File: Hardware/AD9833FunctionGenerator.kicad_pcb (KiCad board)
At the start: 2 copper layers, 125.7 x 172.7 mm, 54 parts, among them U1 LM7805_TO220

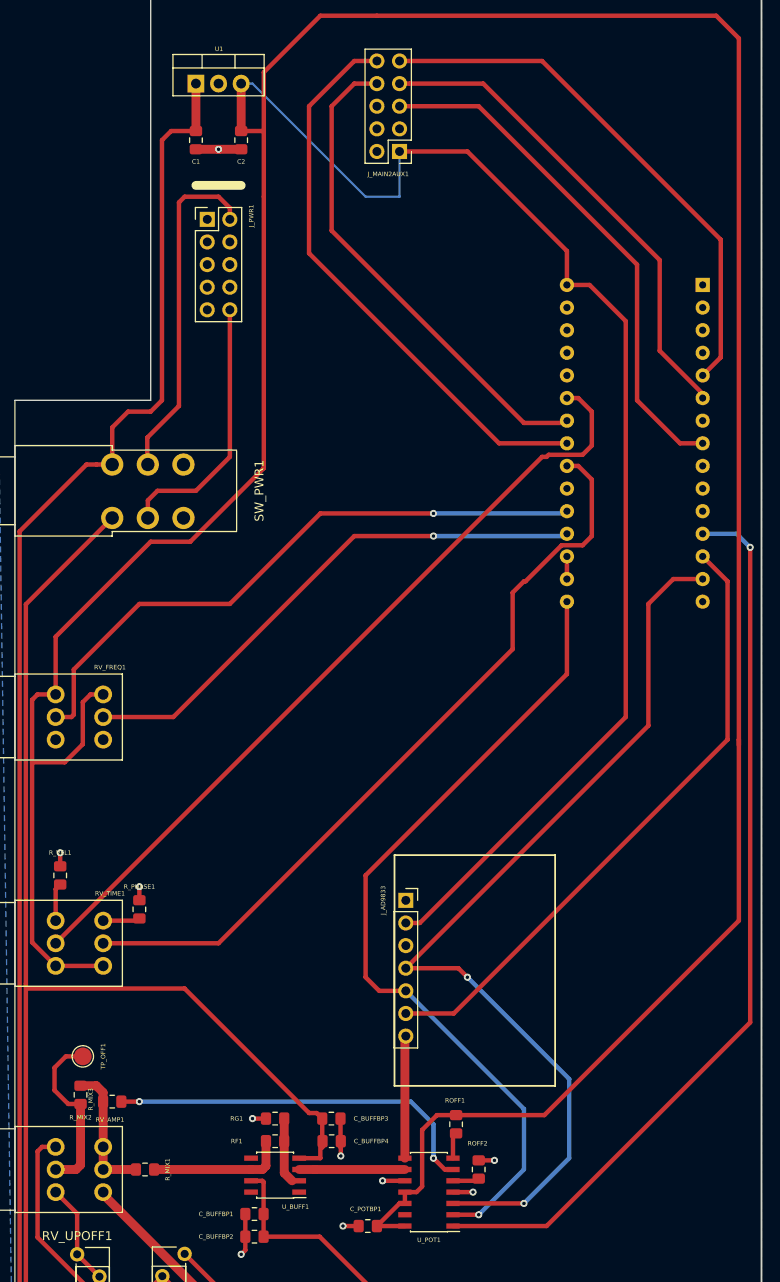
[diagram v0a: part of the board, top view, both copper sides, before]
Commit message: Repositioned Nano module so that USB socket faces upwards
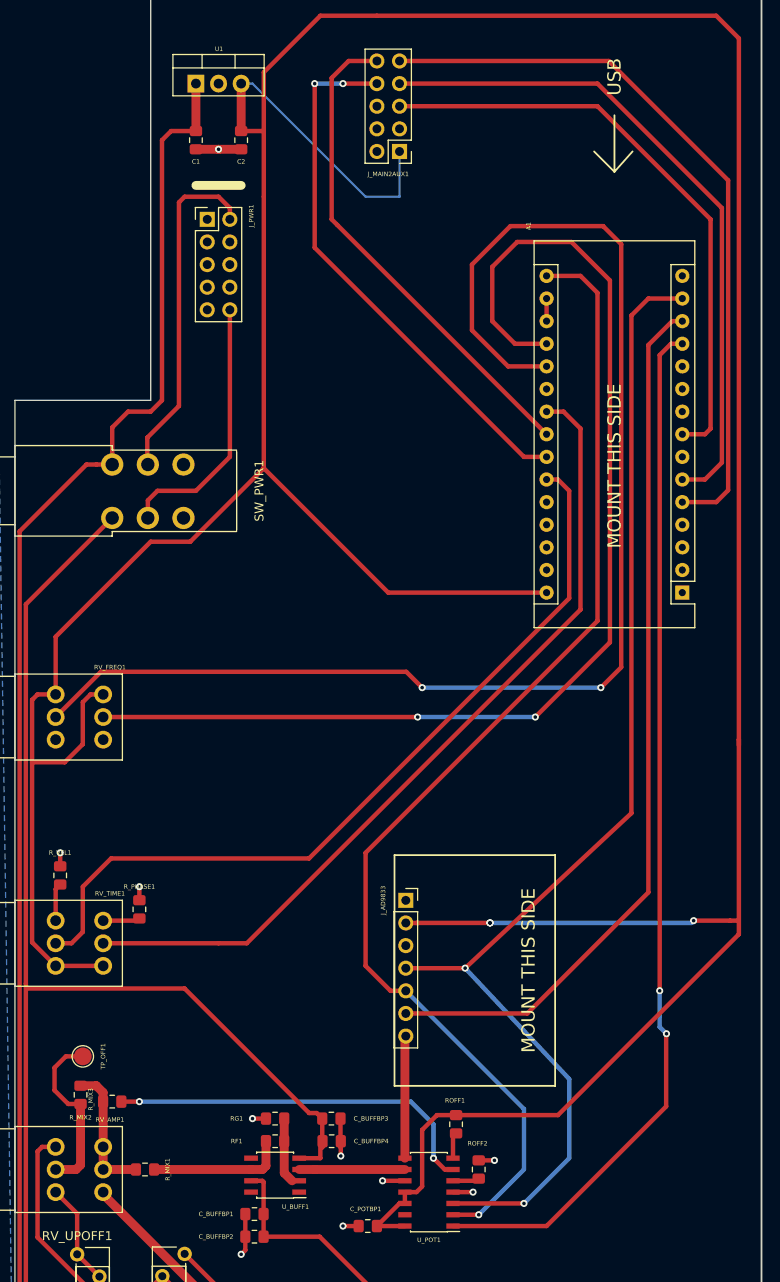
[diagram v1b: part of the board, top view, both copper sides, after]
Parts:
- A1: moved to F.Cu
- moved A1 34.6 mm to (141.0, 87.6)
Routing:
- net /FREQLO: track 70.0 -> 151.6 mm, vias 1 -> 2
- net /FREQHI: track 60.6 -> 130.4 mm, vias 1 -> 2
- net /SCK: track 92.3 -> 134.2 mm
- net /5V: track 505.0 -> 466.7 mm, vias 0 -> 3
- net /MOSI: track 107.0 -> 135.7 mm
- net /DDS_CS: track 70.6 -> 99.2 mm
- net /WAVEBTN: track 60.5 -> 82.9 mm
- net /MODEBTN: track 54.9 -> 75.8 mm
- net /POT_CS: track 102.1 -> 117.3 mm, vias 1 -> 2
- net /RANGEBTN: track 58.6 -> 67.1 mm
- net /SDA: track 64.0 -> 55.9 mm
- net /PHASE1: track 87.3 -> 94.0 mm
- net /SCL: track 55.6 -> 61.2 mm, vias 0 -> 2
- net /VEL1: track 90.6 -> 91.8 mm
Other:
- board text added: "MOUNT THIS SIDE"
- board text added: "USB"

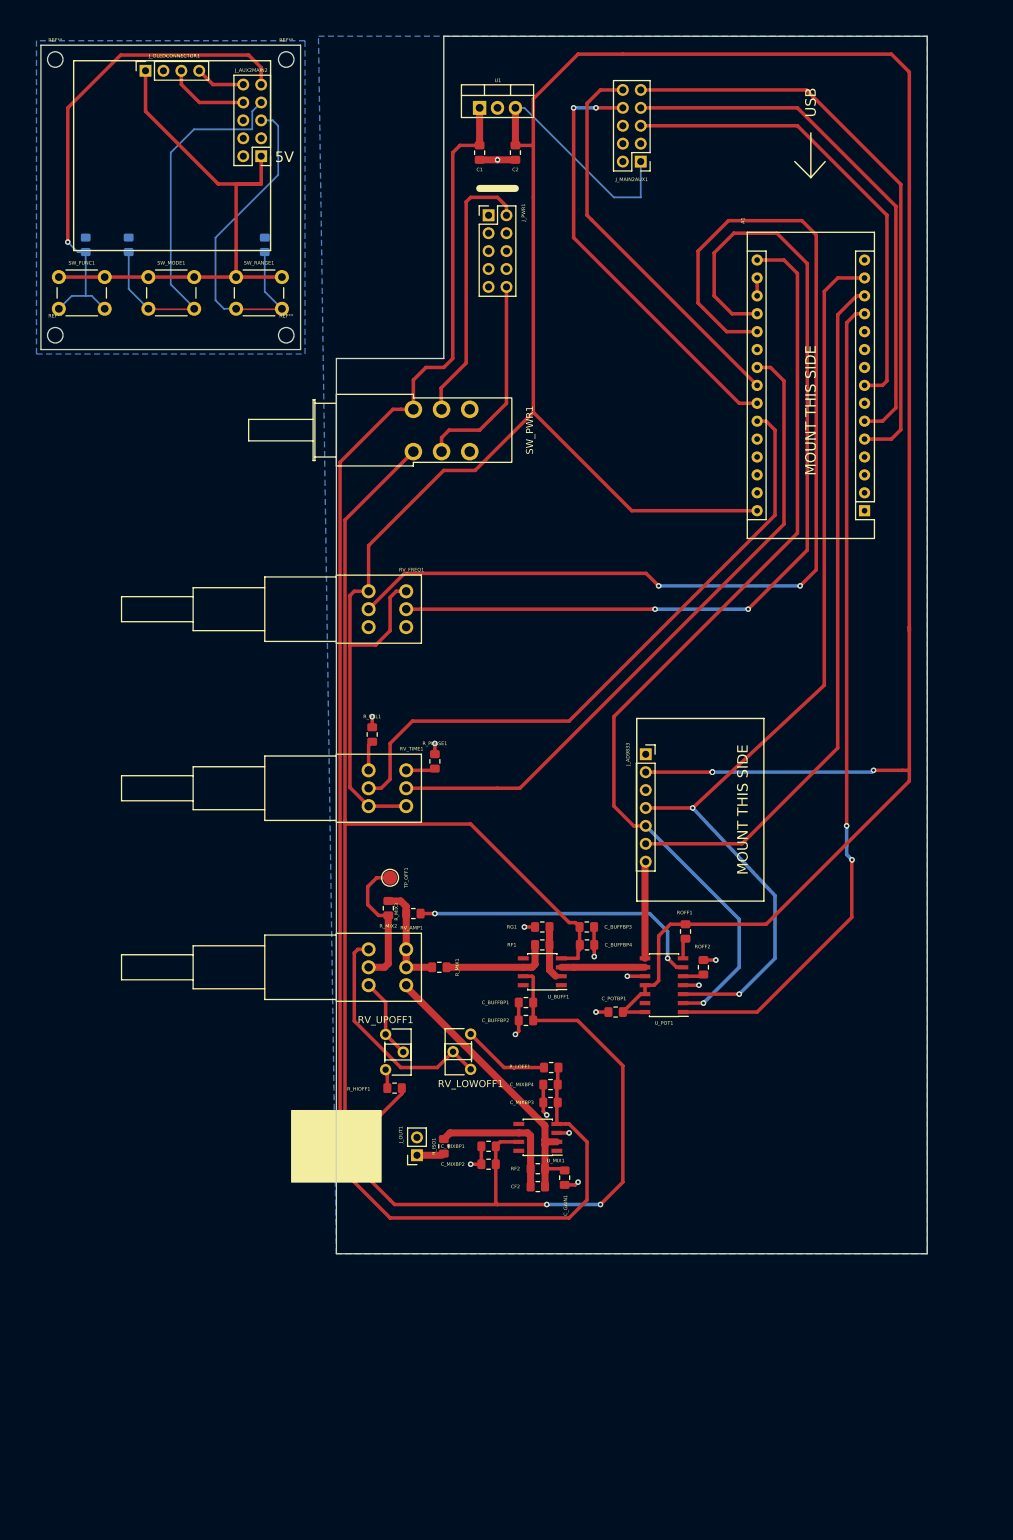
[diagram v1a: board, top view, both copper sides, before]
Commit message: Reduced size of board width to 90mm
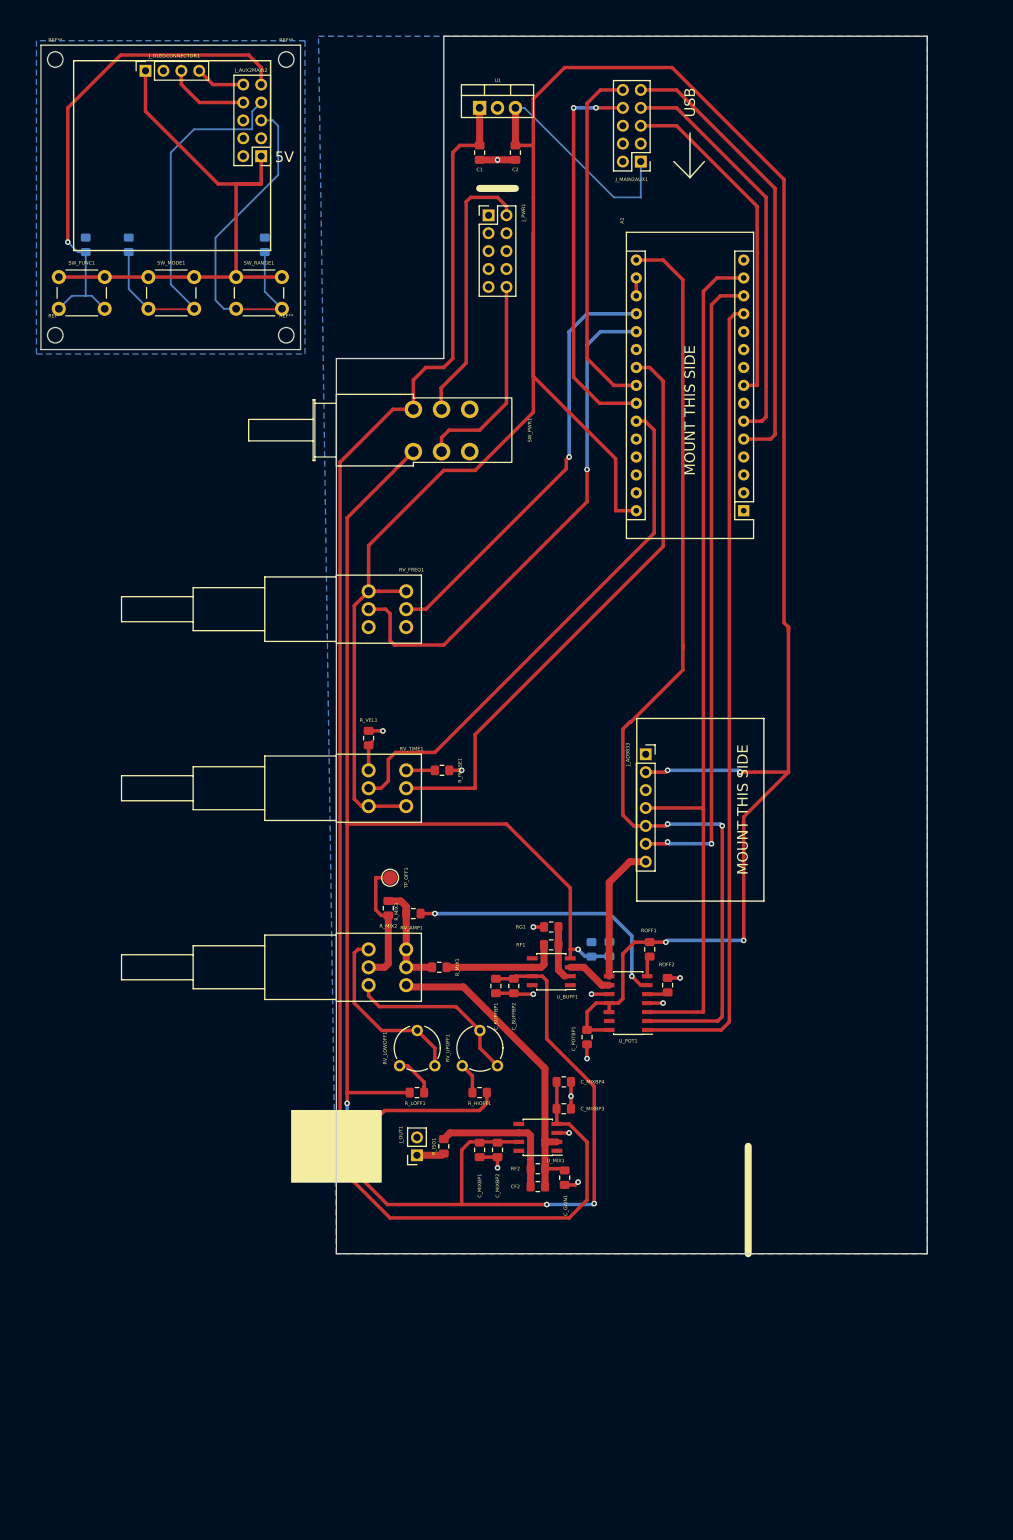
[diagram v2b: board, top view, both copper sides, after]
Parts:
- C_BUFFBP3, C_BUFFBP4: moved to B.Cu
- RV_LOWOFF1, RV_UPOFF1: footprint Potentiometer_THT:Potentiometer_Piher_PT-6-H_Horizontal -> Potentiometer_THT:Potentiometer_Piher_PT-6-V_Vertical
- moved R_LOFF1 19.4 mm to (77.5, 170.2), turned to 0 degrees
- moved A1 17.1 mm to (123.8, 87.6)
- moved RV_UPOFF1 16.5 mm to (88.9, 166.4), turned to 90 degrees
- moved R_HIOFF1 12.1 mm to (86.4, 170.2)
- moved ROFF1 5.68 mm to (110.5, 149.9)
- moved U_POT1 5.68 mm to (107.4, 157.5)
- moved ROFF2 5.68 mm to (113.0, 154.9)
- moved C_POTBP1 5.39 mm to (101.6, 162.3), turned to 270 degrees
- moved C_BUFFBP2 5.18 mm to (91.2, 155.1), turned to 270 degrees
- moved RV_LOWOFF1 5.11 mm to (80.0, 166.4), turned to 90 degrees
- moved C_BUFFBP1 4.87 mm to (88.7, 155.1), turned to 270 degrees
- moved C_BUFFBP3 4.49 mm to (104.8, 149.8), turned to 90 degrees
- moved C_MIXBP2 2.40 mm to (88.9, 178.3), turned to 270 degrees
- moved C_MIXBP3 2.08 mm to (98.3, 172.5), turned to 0 degrees
- moved C_MIXBP4 1.92 mm to (98.3, 168.7), turned to 0 degrees
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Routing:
- net /FREQLO: track 151.6 -> 73.7 mm, vias 2 -> 1
- net /FREQHI: track 130.4 -> 61.2 mm, vias 2 -> 1
- net /5V: track 466.7 -> 422.7 mm, vias 3 -> 4
- net /RANGEBTN: track 67.1 -> 48.5 mm
- net /WAVEBTN: track 82.9 -> 64.5 mm
- net /MODEBTN: track 75.8 -> 57.6 mm
- net /+12V: track 268.1 -> 285.0 mm
- net /VEL1: track 91.8 -> 75.0 mm
- net Net-(RV_AMP1-Pad1): track 11.5 -> 25.4 mm
- net /PHASE1: track 94.0 -> 83.2 mm
- net /MOSI: track 135.7 -> 125.3 mm, vias 2 -> 0
- net /-12V: track 213.3 -> 223.6 mm, vias 2 -> 3
- net /DDS_CS: track 99.2 -> 91.1 mm, vias 0 -> 2
- net Net-(RV_AMP1-Pad3): track 33.1 -> 25.9 mm
- net /SCK: track 134.2 -> 140.7 mm, vias 1 -> 2
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
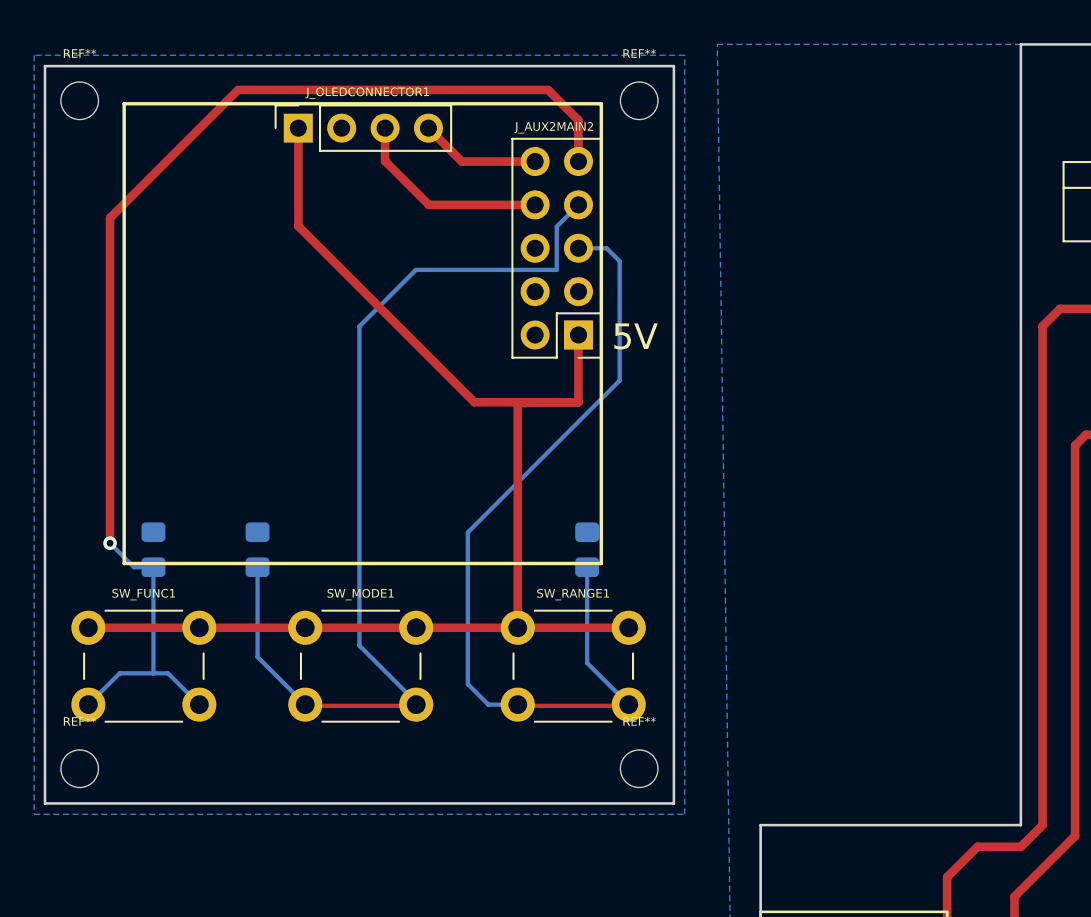
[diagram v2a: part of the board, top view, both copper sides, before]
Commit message: Reduced size of board width to 90mm
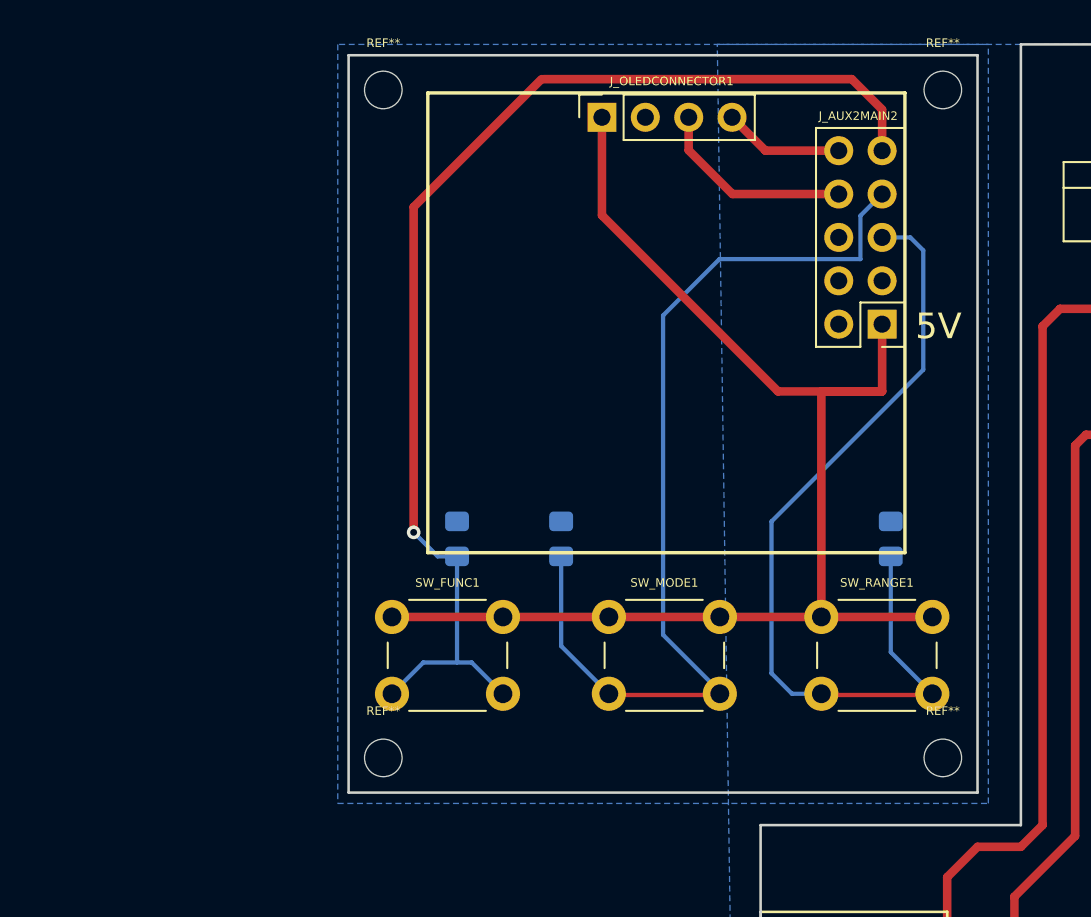
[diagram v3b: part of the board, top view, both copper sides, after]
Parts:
- moved J_AUX2MAIN2 17.8 mm to (73.2, 36.7)
- moved J_OLEDCONNECTOR1 17.8 mm to (56.7, 24.6)
- moved REF** 17.8 mm to (43.9, 23.0)
- moved REF** 17.8 mm to (76.7, 23.0)
- moved REF** 17.8 mm to (76.7, 62.1)
- moved REF** 17.8 mm to (43.9, 62.1)
- moved R_MODE1 17.8 mm to (54.4, 49.3)
- moved SW_FUNC1 17.8 mm to (44.5, 53.8)
- moved SW_MODE1 17.8 mm to (57.1, 53.8)
- moved SW_RANGE1 17.8 mm to (69.6, 53.8)
- moved R_FUNC1 17.8 mm to (48.3, 49.3)
- moved R_RANGE1 17.8 mm to (73.7, 49.3)
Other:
- board size 125.7 x 172.7 mm -> 108 x 172.7 mm

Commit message: Refined board layout
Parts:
- C_BUFFBP1, C_BUFFBP2, C_MIXBP1, C_MIXBP2, C_MIXBP3, C_MIXBP4, C_POTBP1: moved to B.Cu
- moved SW_RANGE1 21.1 mm to (48.6, 51.3)
- moved REF** 21.1 mm to (23.0, 20.4)
- moved REF** 21.1 mm to (23.0, 59.6)
- moved SW_FUNC1 21.1 mm to (23.5, 51.3)
- moved J_AUX2MAIN2 21.1 mm to (52.2, 34.2)
- moved J_OLEDCONNECTOR1 21.1 mm to (35.8, 22.0)
- moved REF** 21.1 mm to (55.8, 20.4)
- moved REF** 21.1 mm to (55.8, 59.6)
- moved R_FUNC1 21.1 mm to (27.3, 46.7)
- moved R_MODE1 21.1 mm to (33.4, 46.7)
- moved R_RANGE1 21.1 mm to (52.7, 46.7)
- moved SW_MODE1 21.1 mm to (36.2, 51.3)
- moved R_MIX3 13.2 mm to (80.6, 157.5)
- moved C_BUFFBP3 5.44 mm to (100.3, 146.7)
- moved C_MIXBP4 3.92 mm to (101.6, 170.8), turned to 90 degrees
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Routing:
- net /OFFSETADJUST: track 39.7 -> 118.2 mm
- net /FREQHI: track 61.2 -> 86.4 mm, vias 1 -> 2
- net /FREQLO: track 73.7 -> 91.7 mm, vias 1 -> 2
- net /5V: track 422.7 -> 438.5 mm, vias 4 -> 5
- net Net-(RV_AMP1-Pad5): track 15.2 -> 27.2 mm
- net /GND: track 35.5 -> 26.3 mm, vias 13 -> 9
- net /SDA: track 50.6 -> 57.6 mm
- net /SCL: track 55.6 -> 62.3 mm
- net /SCK: track 140.7 -> 142.7 mm
- net Net-(RV_AMP1-Pad3): track 25.9 -> 24.1 mm
- net /MOSI: track 125.3 -> 123.6 mm
- net Net-(RV_AMP1-Pad1): track 25.4 -> 24.1 mm
- net /-12V: track 223.6 -> 224.4 mm, vias 3 -> 4
- net /PHASE1: track 83.2 -> 82.4 mm
- net /+12V: track 285.0 -> 285.6 mm, vias 2 -> 4
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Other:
- board size 108 x 172.7 mm -> 110.6 x 174.6 mm

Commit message: Refined board layout
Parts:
- removed the REF** at (23.0, 20.4)
- removed the REF** at (55.8, 20.4)
- removed the REF** at (55.8, 59.6)
- removed the REF** at (23.0, 59.6)
- added REF**: MountingHole_2.2mm_M2_ISO7380, MountingHole:MountingHole_2.2mm_M2_ISO7380, F.Cu at (50.8, 38.1)
- added REF**: MountingHole_2.2mm_M2_ISO7380, MountingHole:MountingHole_2.2mm_M2_ISO7380, F.Cu at (83.8, 38.1)
- added REF**: MountingHole_2.2mm_M2_ISO7380, MountingHole:MountingHole_2.2mm_M2_ISO7380, F.Cu at (83.8, 77.5)
- added REF**: MountingHole_2.2mm_M2_ISO7380, MountingHole:MountingHole_2.2mm_M2_ISO7380, F.Cu at (50.8, 77.5)
- moved R_MIX3 62.0 mm to (141.0, 171.7), turned to 90 degrees
- moved ROFF1 40.3 mm to (135.3, 181.6), turned to 180 degrees
- moved ROFF2 35.5 mm to (144.3, 171.7), turned to 270 degrees
- moved R_MIX2 33.3 mm to (101.1, 162.6), turned to 0 degrees
- moved CF2 33.1 mm to (122.6, 201.3)
- moved C_BUFFBP3 33.1 mm to (128.3, 164.5)
- moved RF2 33.1 mm to (122.6, 198.8)
- moved R_FUNC1 33.1 mm to (55.2, 64.5)
- moved R_HIOFF1 33.1 mm to (113.3, 188.0)
- moved R_MODE1 33.1 mm to (61.3, 64.5)
- moved R_PHASE1 33.1 mm to (109.0, 142.2)
- moved R_RANGE1 33.1 mm to (80.6, 64.5)
- moved R_VEL1 33.1 mm to (98.6, 137.7)
- moved U_MIX1 33.1 mm to (122.6, 194.3)
- moved U_POT1 33.1 mm to (135.4, 175.3)
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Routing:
- net /OFFSETADJUST: track 118.2 -> 2.89 mm, vias 2 -> 0
- net Net-(RV_AMP1-Pad5): track 27.2 -> 70.3 mm, vias 0 -> 2
- net /+12V: track 285.6 -> 322.3 mm, vias 4 -> 2
- net /5V: track 438.5 -> 472.0 mm, vias 5 -> 3
- net Net-(ROFF1-Pad1): track 2.93 -> 12.9 mm
- net Net-(ROFF2-Pad1): track 2.99 -> 9.20 mm
- net /GND: track 26.3 -> 32.0 mm, vias 9 -> 8
- net Net-(RV_AMP1-Pad2): track 18.6 -> 15.7 mm
- net /-12V: track 224.4 -> 226.1 mm
- net /DDS_SIG: track 19.8 -> 18.5 mm

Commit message: Draft RevA Board
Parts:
- added CF1: 2pF, Capacitor_SMD:C_0805_2012Metric_Pad1.15x1.40mm_HandSolder, F.Cu at (95.5, 186.4)
- moved U1 41.9 mm to (95.2, 85.6)
- moved C1 40.1 mm to (95.2, 89.9)
- moved C2 40.1 mm to (100.3, 89.9)
- moved R_HIOFF1 39.3 mm to (81.3, 210.8)
- moved RV_UPOFF1 39.1 mm to (83.9, 207.0)
- moved J_PWR1 38.1 mm to (96.5, 96.5)
- moved C_BUFFBP1 37.8 mm to (86.1, 195.7)
- moved C_BUFFBP2 37.6 mm to (88.9, 195.7)
- moved RV_LOWOFF1 37.6 mm to (76.2, 207.0)
- moved R_LOFF1 37.6 mm to (73.7, 210.8)
- moved C_BUFFBP3 36.9 mm to (99.3, 187.3)
- moved U_BUFF1 36.9 mm to (95.5, 193.7)
- moved C_BUFFBP4 36.9 mm to (101.9, 187.3)
- moved R_PHASE1 36.6 mm to (77.2, 160.5), turned to 270 degrees
- moved RF1 36.5 mm to (95.5, 189.2)
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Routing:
- net /5V: track 472.0 -> 446.0 mm
- net /PHASE1: track 82.4 -> 97.6 mm
- net /VEL1: track 75.5 -> 88.9 mm
- net /AuxiliaryBoard/MODEBTN_AUX: track 56.2 -> 64.6 mm
- net Net-(CF2-Pad1): track 20.1 -> 11.9 mm
- net /RANGEBTN: track 48.5 -> 40.5 mm
- net /MODEBTN: track 57.6 -> 50.1 mm
- net /WAVEBTN: track 64.5 -> 57.2 mm
- net /OutputSection/SIGOUT: track 3.91 -> 10.0 mm
- net Net-(RV_AMP1-Pad1): track 24.1 -> 18.1 mm
- net /FREQHI: track 86.4 -> 80.6 mm
- net Net-(J_PWR1-Pad10): track 29.7 -> 23.9 mm
- net /FREQLO: track 91.7 -> 86.2 mm
- net /SDA: track 57.6 -> 62.3 mm
- net /SCK: track 142.7 -> 146.8 mm
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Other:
- board size 110.6 x 174.6 mm -> 90.7 x 167.6 mm
- board text added: "OUT"
- board text added: "PLUG THIS SIDE"
- board text removed: "5V"
